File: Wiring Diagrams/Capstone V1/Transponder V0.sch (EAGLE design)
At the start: 19 parts, among them IC2 74LS125N

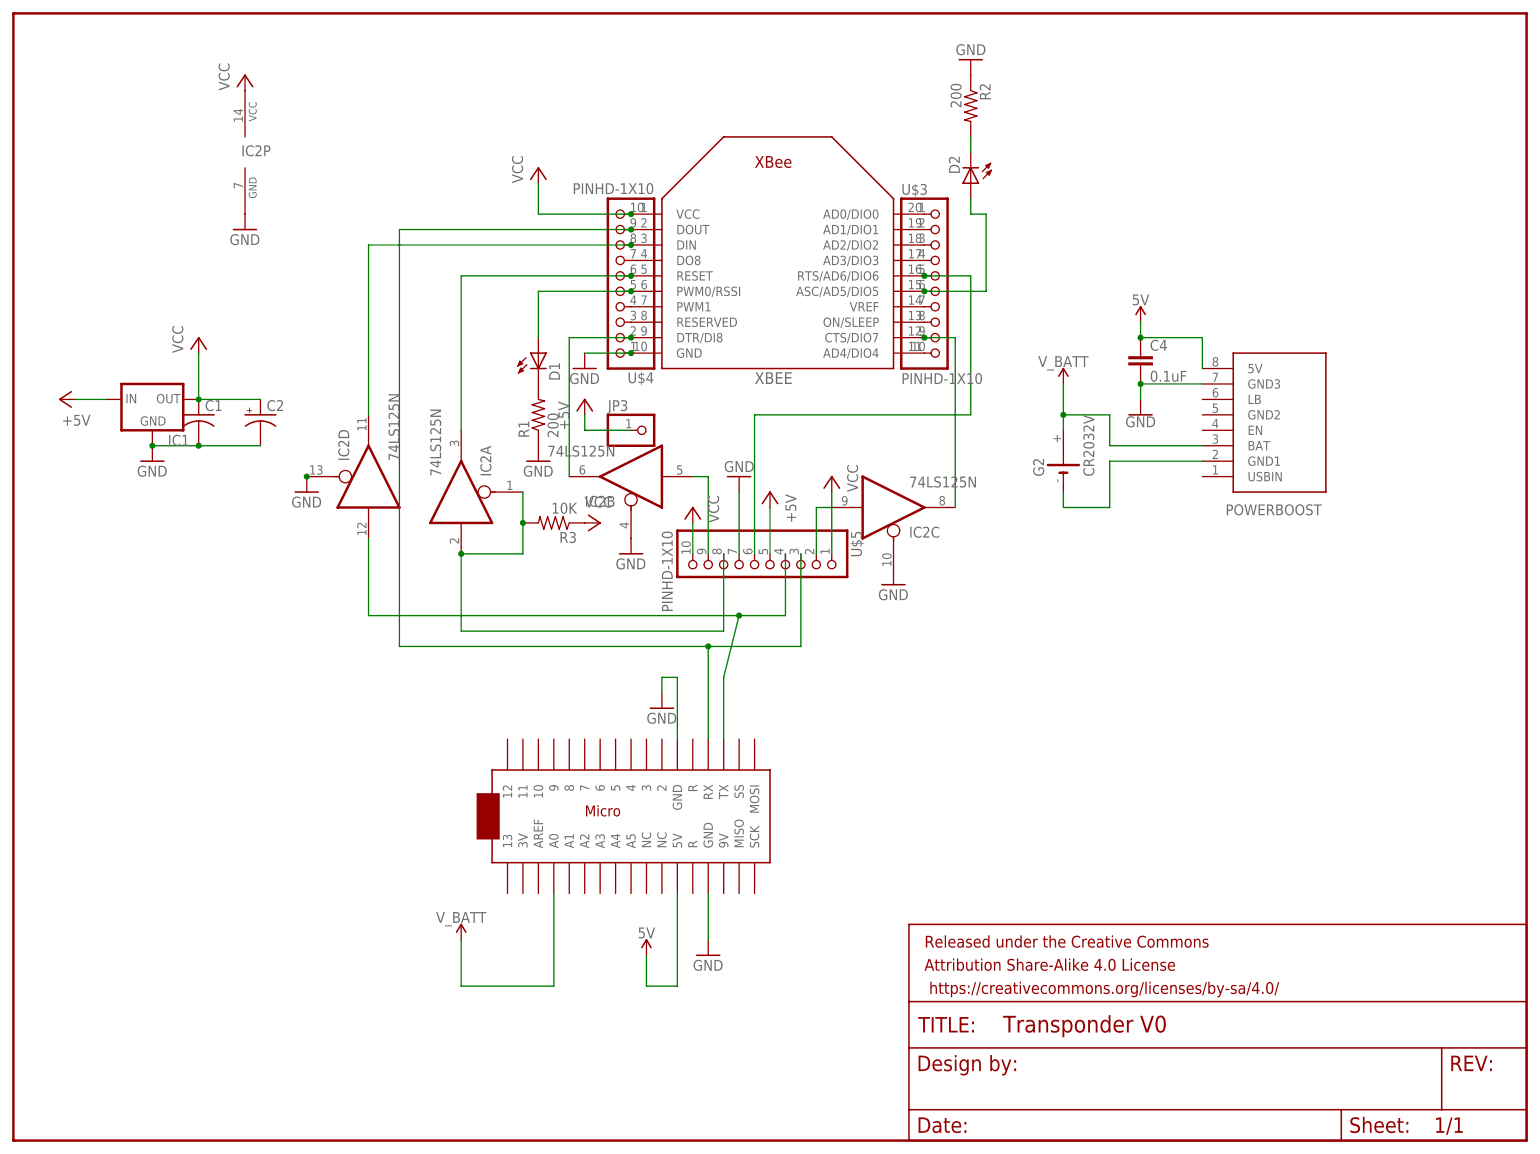
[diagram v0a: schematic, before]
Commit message: Reorganized wire diagram files, added rover diagrams
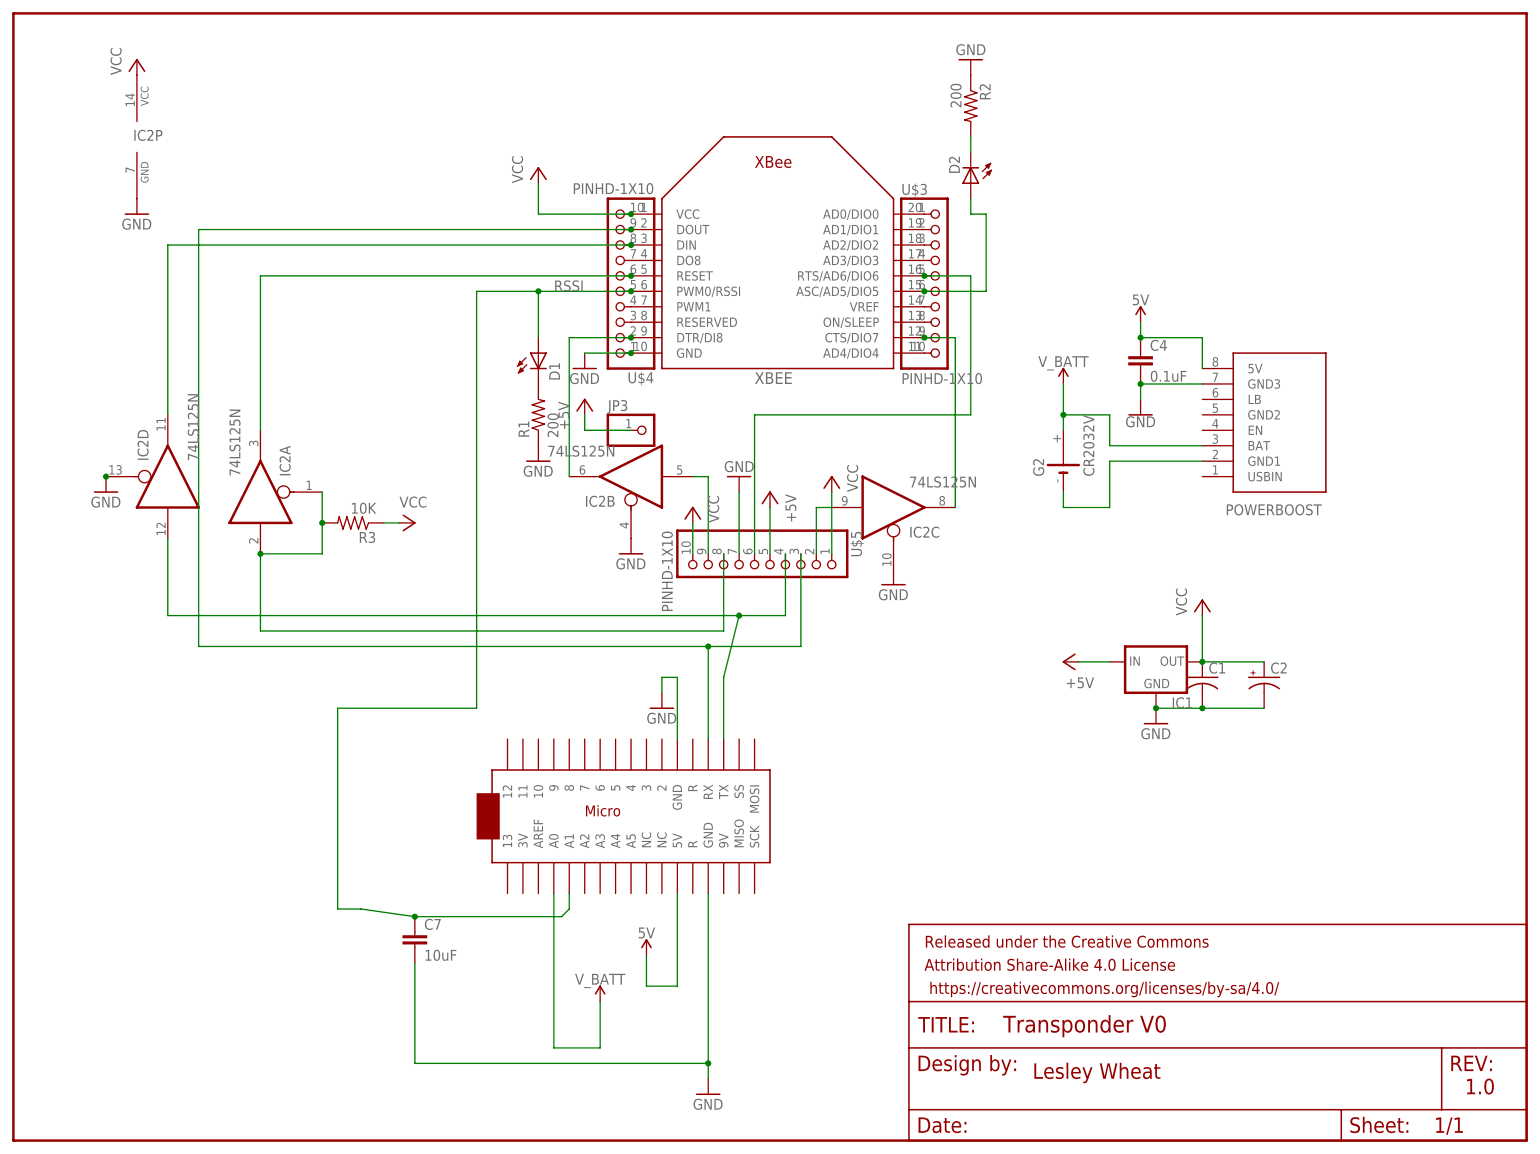
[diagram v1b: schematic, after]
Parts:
- added C7: 10uF, SparkFun-Capacitors:10UF-0603-6.3V-20%
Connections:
- removed net N$7: D1.A, U$4.5, XBEE.PWM0/RSSI
- new net RSSI: C7.1, D1.A, U$2.A1, U$4.5, XBEE.PWM0/RSSI
- net GND: now also C7.2
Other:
- note added: "1.0"
- note added: "Lesley Wheat"
- moved on the sheet: C1, C2, IC1, IC2A, IC2D, IC2P, R3
